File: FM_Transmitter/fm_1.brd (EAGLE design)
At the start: 46.7 x 38.1 mm, 15 parts, among them T1 2N3904, T2 2N3904

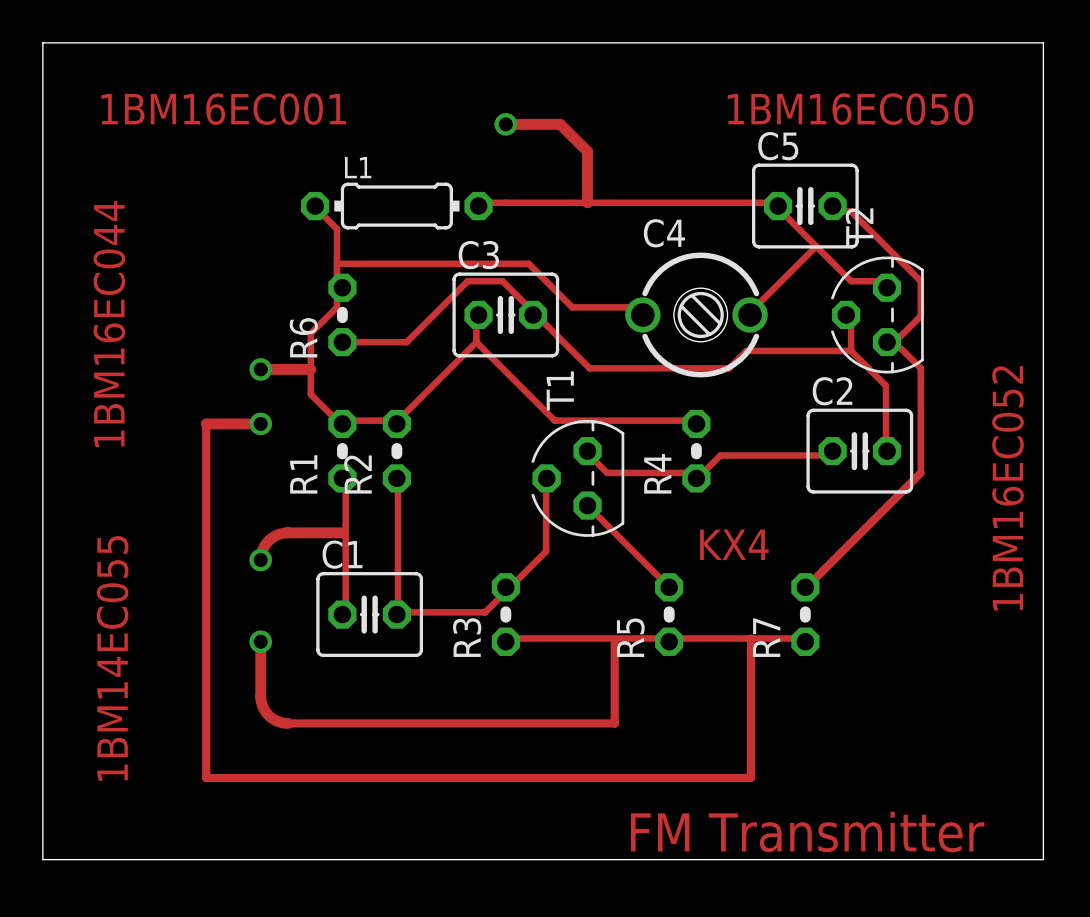
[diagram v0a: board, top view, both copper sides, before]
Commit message: changed to 3pin Trimmer Cap + USN's corrected
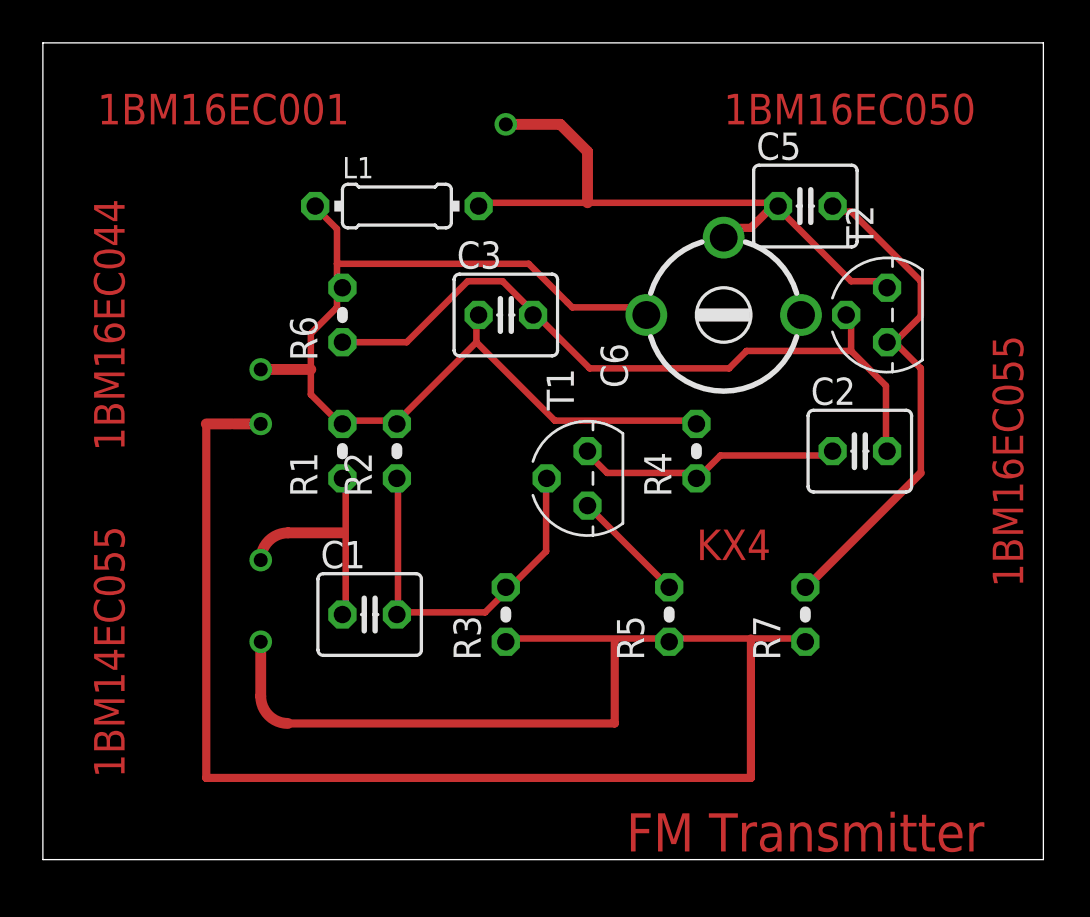
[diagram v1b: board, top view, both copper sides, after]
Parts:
- removed C4: 4-40pF, rcl:CTRIM3050.505
- added C6: (no value), rcl:CTRIM808-BC
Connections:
- net N$1: now also C6.1; no longer C4.1
- net N$7: now also C6.2; no longer C4.2
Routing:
- net N$7: track 27.7 -> 26.5 mm
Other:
- board text added: "1BM16EC055"
- board text removed: "1BM16EC052"
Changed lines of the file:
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@@
 <layers>
 <layer number="1" name="Top" color="4" fill="1" visible="yes" active="yes"/>
-<layer number="16" name="Bottom" color="1" fill="1" visible="no" active="yes"/>
+<layer number="16" name="Bottom" color="1" fill="1" visible="yes" active="yes"/>
 <layer number="17" name="Pads" color="2" fill="1" visible="yes" active="yes"/>
 <layer number="18" name="Vias" color="2" fill="1" visible="yes" active="yes"/>
@@
 <text x="3.81" y="19.05" size="1.4224" layer="1" ratio="0" rot="R90">1BM16EC044</text>
 <text x="31.75" y="34.29" size="1.4224" layer="1" ratio="0">1BM16EC050</text>
-<text x="45.72" y="11.43" size="1.4224" layer="1" ratio="0" rot="R90">1BM16EC052</text>
-<text x="2.54" y="15.24" size="1.4224" layer="1" ratio="0" rot="R270">1BM14EC055</text>
+<text x="3.81" y="3.81" size="1.4224" layer="1" rot="R90">1BM14EC055</text>
+<text x="45.72" y="12.7" size="1.4224" layer="1" rot="R90">1BM16EC055</text>
 </plain>
 <attributes>
@@
 <attribute name="VALUE" x="19.304" y="21.971" size="1.27" layer="27" ratio="10"/>
 </element>
-<element name="C4" library="rcl" library_urn="urn:adsk.eagle:library:334" package="CTRIM3050.505" package3d_urn="urn:adsk.eagle:package:23773/1" value="4-40pF" x="30.48" y="25.4" smashed="yes">
-<attribute name="NAME" x="27.94" y="28.575" size="1.27" layer="25"/>
-<attribute name="SPICEPREFIX" value="C" x="46.99" y="20.32" size="1.778" layer="27" display="off"/>
-<attribute name="VALUE" x="27.94" y="20.955" size="1.27" layer="27"/>
-</element>
 <element name="C5" library="rcl" library_urn="urn:adsk.eagle:library:334" package="C025-040X050" package3d_urn="urn:adsk.eagle:package:23634/1" value="4.7pF" x="35.56" y="30.48" smashed="yes">
 <attribute name="NAME" x="33.274" y="32.639" size="1.27" layer="25" ratio="10"/>
@@
 <attribute name="VALUE" x="40.64" y="28.575" size="1.27" layer="27" ratio="10" rot="R90"/>
 </element>
+<element name="C6" library="rcl" library_urn="urn:adsk.eagle:library:334" package="CTRIM808-BC" package3d_urn="urn:adsk.eagle:package:23766/1" value="" x="31.75" y="25.4" smashed="yes">
+<attribute name="NAME" x="27.2816" y="21.9944" size="1.27" layer="25" rot="R90"/>
+<attribute name="SPICEPREFIX" value="C" x="31.75" y="25.4" size="1.778" layer="27" display="off"/>
+<attribute name="VALUE" x="37.52" y="21.9944" size="1.27" layer="27" rot="R90"/>
+</element>
 </elements>
 <signals>
 <signal name="N$1">
 <contactref element="R1" pad="2"/>
-<contactref element="C4" pad="1"/>
 <contactref element="L1" pad="1"/>
 <contactref element="R2" pad="2"/>
@@
 <wire x1="12.9032" y1="30.226" x2="12.7" y2="30.48" width="0.3048" layer="1"/>
 <wire x1="24.6888" y1="25.7556" x2="27.94" y2="25.7556" width="0.3048" layer="1"/>
-<wire x1="22.6568" y1="27.7876" x2="24.6888" y2="25.7556" width="0.3048" layer="1"/>
+<wire x1="22.6568" y1="27.7876" x2="24.4602" y2="25.9842" width="0.3048" layer="1"/>
+<wire x1="24.4602" y1="25.9842" x2="24.6888" y2="25.7556" width="0.3048" layer="1"/>
 <wire x1="13.716" y1="27.7876" x2="22.6568" y2="27.7876" width="0.3048" layer="1"/>
-<wire x1="27.94" y1="25.7556" x2="27.98" y2="25.4" width="0.3048" layer="1"/>
 <wire x1="16.1544" y1="20.4724" x2="14.1224" y2="20.4724" width="0.3048" layer="1"/>
 <wire x1="14.1224" y1="20.4724" x2="13.97" y2="20.32" width="0.3048" layer="1"/>
@@
 <wire x1="13.716" y1="20.4724" x2="13.97" y2="20.32" width="0.3048" layer="1"/>
 <wire x1="12.4968" y1="22.86" x2="10.16" y2="22.86" width="0.508" layer="1"/>
-<wire x1="13.716" y1="26.67" x2="13.716" y2="26.924" width="0" layer="19" extent="1-1"/>
+<contactref element="C6" pad="1"/>
+<wire x1="13.716" y1="26.924" x2="13.97" y2="26.67" width="0.508" layer="1"/>
+<wire x1="27.94" y1="25.7556" x2="28.1432" y2="25.4" width="0" layer="19" extent="1-1"/>
 </signal>
 <signal name="N$2">
@@
 </signal>
 <signal name="N$7">
-<contactref element="C4" pad="2"/>
 <contactref element="T2" pad="1"/>
 <contactref element="L1" pad="2"/>
 <contactref element="C5" pad="1"/>
 <wire x1="34.036" y1="30.6324" x2="25.4" y2="30.6324" width="0.3048" layer="1"/>
-<wire x1="25.4" y1="30.6324" x2="21.59" y2="30.6324" width="0.3048" layer="1"/>
-<wire x1="21.59" y1="30.6324" x2="20.6248" y2="30.6324" width="0.3048" layer="1"/>
+<wire x1="25.4" y1="30.6324" x2="20.6248" y2="30.6324" width="0.3048" layer="1"/>
 <wire x1="20.6248" y1="30.6324" x2="20.32" y2="30.48" width="0.3048" layer="1"/>
 <wire x1="34.036" y1="30.6324" x2="34.29" y2="30.48" width="0.3048" layer="1"/>
 <wire x1="37.6936" y1="26.9748" x2="39.3192" y2="26.9748" width="0.3048" layer="1"/>
-<wire x1="34.4424" y1="30.226" x2="36.068" y2="28.6004" width="0.3048" layer="1"/>
-<wire x1="36.068" y1="28.6004" x2="37.6936" y2="26.9748" width="0.3048" layer="1"/>
+<wire x1="34.4424" y1="30.226" x2="37.6936" y2="26.9748" width="0.3048" layer="1"/>
 <wire x1="39.3192" y1="26.9748" x2="39.37" y2="26.67" width="0.3048" layer="1"/>
 <wire x1="34.4424" y1="30.226" x2="34.29" y2="30.48" width="0.3048" layer="1"/>
-<wire x1="36.068" y1="28.6004" x2="33.2232" y2="25.7556" width="0.3048" layer="1"/>
-<wire x1="33.2232" y1="25.7556" x2="32.98" y2="25.4" width="0.3048" layer="1"/>
 <wire x1="25.4" y1="30.6324" x2="25.4" y2="33.02" width="0.508" layer="1"/>
+<contactref element="C6" pad="2"/>
+<wire x1="33.02" y1="29.464" x2="32.004" y2="29.464" width="0.381" layer="1"/>
+<wire x1="34.036" y1="30.48" x2="33.02" y2="29.464" width="0.381" layer="1"/>
+<wire x1="32.004" y1="29.464" x2="31.75" y2="29.0068" width="0.381" layer="1"/>
+<wire x1="34.036" y1="30.48" x2="34.29" y2="30.48" width="0.508" layer="1"/>
 </signal>
 <signal name="N$8">
